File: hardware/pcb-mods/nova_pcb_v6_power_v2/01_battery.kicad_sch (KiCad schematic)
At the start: 4 parts, among them J1 XT60_4S_IN, M1 Voltmeter_DC, Q1 IRLB3034PBF, SW1 Rocker_30A

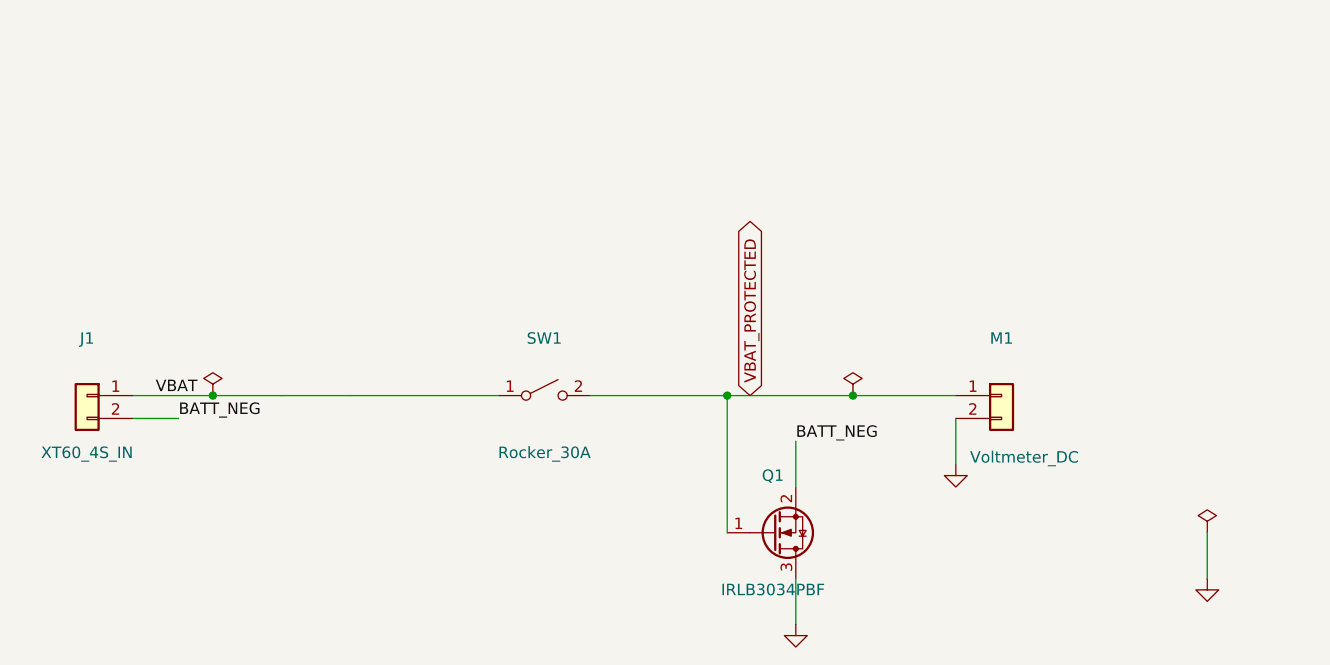
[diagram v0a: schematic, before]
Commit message: boards: fab-ready GO (both) — Q1 gate-harden + soft-start, mounting-hole keepouts, BATT_NEG zone, PWR_FLAG, fresh gerbers (separate NPTH/PTH)
Power v2: Q1 gate soft-start (R17 10k + C_gs 470nF + D1 18V zener + R_gs) on Q1_GATE,
BATT_NEG F.Cu zone (solid to Q1 source, islands merged), 7mm copper keepout all 4 holes
all layers, GND PWR_FLAG. Logic: 7mm keepout all 4 holes (V5_AUX was 0.4mm from barrel).
Both: gerbers regenerated w/ explicit layer set + separate PTH/NPTH drill (M3 holes stay
non-plated). fab_gate GO: ERC 0 / DRC 0 hard / J20 match / DNP U5+U12.

Co-Authored-By: Claude Opus 4.8 <noreply@anthropic.com>
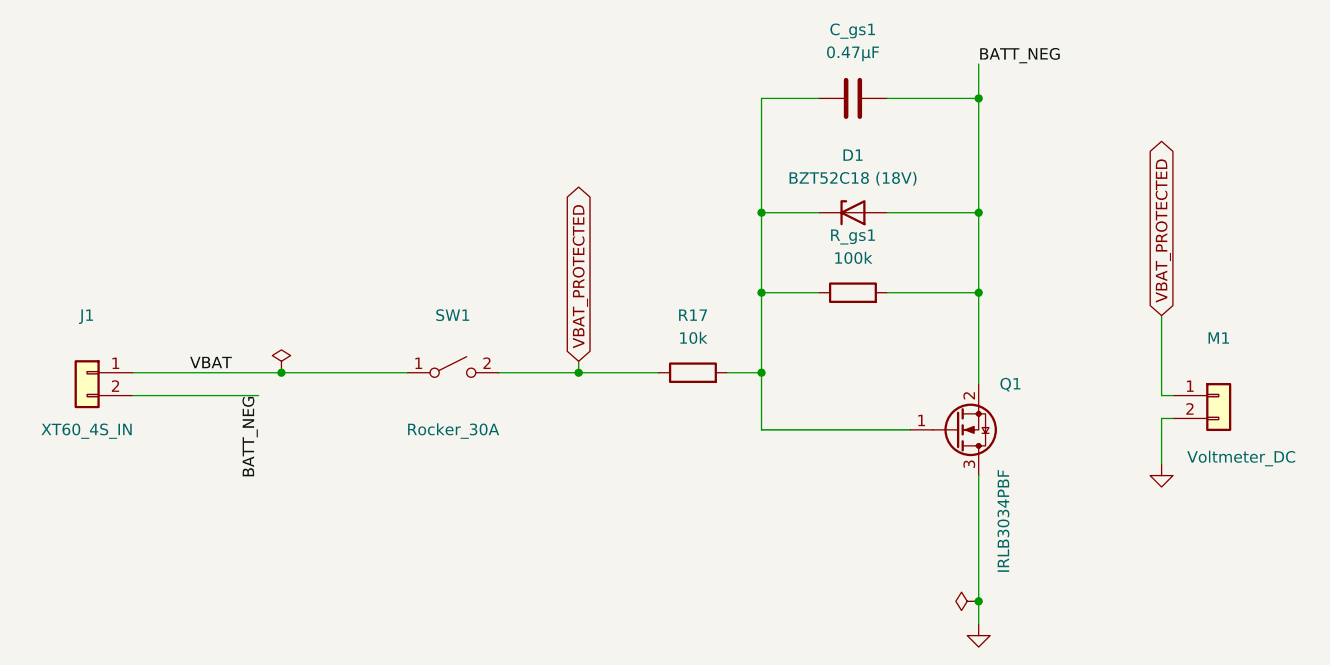
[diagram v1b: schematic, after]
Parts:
- added C_gs1: 0.47μF, Capacitor_SMD:C_0603_1608Metric, symbol Device:C
- added D1: BZT52C18 (18V), Diode_SMD:D_SOD-123F, symbol Device:D_Zener
- added R17: 10k, Resistor_SMD:R_0603_1608Metric, symbol Device:R
- added R_gs1: 100k, Resistor_SMD:R_0603_1608Metric, symbol Device:R
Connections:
- net BATT_NEG: now also C_gs1.2, D1.2 (A), R_gs1.2
- net VBAT_PROTECTED: now also R17.1; no longer Q1.1 (G)
- new net: C_gs1.1, D1.1 (K), Q1.1 (G), R17.2, R_gs1.1
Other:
- moved on the sheet: J1, M1, Q1, SW1

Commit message: power board: fix reversed XT connector polarity (all 9 AMASS XT)
AMASS XT footprints number pad1=chamfer/NEGATIVE, pad2=flat/POSITIVE.
Board had +V wired to pad1 -> every keyed power connector reverse-wired:
J1 (XT60 battery in), J3-J7 (rail injection), J12-J14 (Jetson/L2/arm out).
Mating a normally-built cable would feed +V to the - terminal and fry the
connected load (Jetson, servos, arm). Confirmed against footprint flat/chamfer
geometry + physical connector (flat=+).

Fix: swapped pin1/pin2 net assignment on all 9 connectors in schematic,
re-routed PCB, regenerated 14-file gerber set. Pololu bucks use a custom
non-keyed terminal (pad1=rect=+V) and were correctly left unchanged.

Verify: ERC 0, DRC 0 hard / 0 unconnected, fab_gate GO, J20 match intact.

Co-Authored-By: Claude Opus 4.8 <noreply@anthropic.com>
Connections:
- net BATT_NEG: now also J1.1 (Pin_1); no longer J1.2 (Pin_2)
- net VBAT: now also J1.2 (Pin_2); no longer J1.1 (Pin_1)
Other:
- moved on the sheet: J1
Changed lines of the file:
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@@
 	(wire
 		(pts
-			(xy 43.18 60.96) (xy 59.69 60.96)
+			(xy 41.91 55.88) (xy 41.91 58.42)
 		)
 		(stroke
@@
 	(wire
 		(pts
-			(xy 43.18 63.5) (xy 57.15 63.5)
-		)
-		(stroke
-			(width 0)
-			(type default)
-		)
-	)
-	(wire
-		(pts
 			(xy 92.71 59.69) (xy 92.71 60.96)
 		)
@@
 	(wire
 		(pts
+			(xy 41.91 60.96) (xy 59.69 60.96)
+		)
+		(stroke
+			(width 0)
+			(type default)
+		)
+	)
+	(wire
+		(pts
 			(xy 109.22 60.96) (xy 113.03 60.96)
 		)
@@
 		(pts
 			(xy 113.03 60.96) (xy 113.03 52.07)
+		)
+		(stroke
+			(width 0)
+			(type default)
+		)
+	)
+	(wire
+		(pts
+			(xy 48.26 55.88) (xy 41.91 55.88)
 		)
 		(stroke
@@
 	)
 	(label "BATT_NEG"
-		(at 57.15 63.5 270)
+		(at 48.26 55.88 0)
 		(effects
 			(font
 				(size 1.27 1.27)
 			)
-			(justify right bottom)
+			(justify left bottom)
 		)
 	)
@@
 	(symbol
 		(lib_id "Connector_Generic:Conn_01x02")
-		(at 38.1 60.96 0)
+		(at 36.83 58.42 0)
 		(mirror y)
 		(unit 1)
@@
 		(dnp no)
 		(property "Reference" "J1"
-			(at 38.1 54.61 0)
+			(at 36.83 52.07 0)
 			(effects
 				(font
@@
 		)
 		(property "Value" "XT60_4S_IN"
-			(at 38.1 67.31 0)
+			(at 36.83 64.77 0)
 			(effects
 				(font
@@
 		)
 		(property "Footprint" "Connector_AMASS:AMASS_XT60-M_1x02_P7.20mm_Vertical"
-			(at 38.1 60.96 0)
+			(at 36.83 58.42 0)
 			(effects
 				(font
@@
 		)
 		(property "Datasheet" "~"
-			(at 38.1 60.96 0)
+			(at 36.83 58.42 0)
 			(effects
 				(font
@@
 		)
 		(property "Description" ""
-			(at 38.1 60.96 0)
+			(at 36.83 58.42 0)
 			(effects
 				(font
@@
 		)
 		(property "Manufacturer" "AMASS"
-			(at 0 -2.54 0)
+			(at -1.27 -5.08 0)
 			(effects
 				(font
@@
 		)
 		(property "MPN" "XT60H-M"
-			(at 0 -2.54 0)
+			(at -1.27 -5.08 0)
 			(effects
 				(font
@@
 		)
 		(property "AssemblyOrder" "12 THT XT60 (snap cover off first)"
-			(at 0 -2.54 0)
-			(effects
-				(font
+			(at -1.27 -5.08 0)
+			(effects
+				(font
